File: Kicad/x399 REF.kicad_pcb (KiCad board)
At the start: 2 copper layers, 106 x 56 mm, 84 parts, among them J1 +15V, J2 Guard, J3 10Vref, Q1 MMBT3904, Q2 2SD882, Q3 AON7410, U1 LM399, U2 OP07

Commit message: Add files via upload
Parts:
- added F1alt1: RXEF010, OwnStuff:RXEF010, F.Cu at (71.0, 78.8)
- added R13alt1: 0.6W tht, Resistor_THT:R_Axial_DIN0309_L9.0mm_D3.2mm_P12.70mm_Horizontal, F.Cu at (167.4, 85.1)
- added R13alt2: 1206 smd, Resistor_SMD:R_1206_3216Metric_Pad1.30x1.75mm_HandSolder, F.Cu at (167.4, 91.4)
- added R25: 0R, Resistor_SMD:R_0805_2012Metric_Pad1.20x1.40mm_HandSolder, B.Cu at (136.6, 100.3)
- C18: value 100n NP0 -> 100n
- moved C9 17.1 mm to (143.6, 100.3)
- moved R6 17.1 mm to (143.6, 104.8)
- moved C3 16.7 mm to (136.6, 104.8), turned to -90 degrees
- moved R5 7.16 mm to (132.0, 87.0)
- moved R5alt1 5.92 mm to (125.4, 87.0)
- moved JP2 4.22 mm to (146.7, 85.0)
- moved H3 3.57 mm to (154.5, 101.3)
- moved JP1 3.57 mm to (144.5, 64.2)
- moved TP1 3.57 mm to (146.6, 68.7)
- moved C1 3.57 mm to (84.0, 76.0)
- moved C11 3.57 mm to (92.9, 70.6)
- moved C13 3.57 mm to (90.4, 72.0)
- moved C14 3.57 mm to (95.3, 65.0)
- moved C18 3.57 mm to (85.5, 98.5)
- moved C22 3.57 mm to (88.9, 108.5)
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- renumbered H3 to H1, H1 to H2, H2 to H3, R1alt1 to R5alt1
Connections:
- C3 pad 1: +10VREF -> Net-(C3-Pad1)
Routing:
- net MGND: track 343.1 -> 256.7 mm, vias 15 -> 22
- net +10VREF: track 300.7 -> 281.1 mm
- net Net-(R13-Pad2): track 62.6 -> 77.3 mm
- net Net-(JP2-A): track 12.5 -> 24.6 mm
- net Net-(U2A--): track 61.3 -> 71.2 mm
- net Net-(JP1-B): track 8.09 -> 16.0 mm
- net Net-(U2A-+): track 161.4 -> 154.6 mm
- net Net-(F1-Pad2): track 9.99 -> 15.0 mm
- net Net-(C3-Pad1): track 0.00 -> 4.12 mm
- net Net-(J1-Pin_1): track 6.47 -> 9.31 mm
- net Earth: track 83.8 -> 84.5 mm, vias 212 -> 200
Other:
- outline, holes or cut-outs redrawn
- board text added: "21-VII-2025"
- board text added: "REV {dblquote}A{dblquote}"
- board text removed: "10-VII-2025"

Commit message: Add files via upload
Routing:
- net Net-(U2A-+): track 154.6 -> 152.0 mm
- net Guard1: vias 0 -> 8
- added copper zone on F.Cu, net Guard1
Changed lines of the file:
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@@
 		(pcbplotparams
 			(layerselection 0x00000000_00000000_55555555_55555551)
-			(plot_on_all_layers_selection 0x00000000_00000000_00000080_02000002)
+			(plot_on_all_layers_selection 0x00000000_00000000_00000080_02000022)
 			(disableapertmacros no)
 			(usegerberextensions no)
@@
 		(sheetfile "x399 REF.kicad_sch")
 		(attr through_hole)
-		(fp_circle
-			(center -1.4 2.7)
-			(end -1.241886 2.700001)
-			(stroke
-				(width 0.1)
-				(type solid)
-			)
-			(fill yes)
-			(layer "F.SilkS")
-		)
 		(fp_line
 			(start 1.7 1.899999)
@@
 		(start 130.024013 92.5125)
 		(end 135.637177 98.125663)
-		(width 0.4)
+		(width 0.3)
 		(layer "B.Cu")
 		(net 1)
@@
 	)
 	(via
-		(at 154.781352 73.981488)
+		(at 154.663745 74.311151)
 		(size 0.8)
 		(drill 0.4)
@@
 	)
 	(via
-		(at 161.706352 73.079977)
+		(at 161.993297 73)
 		(size 0.8)
 		(drill 0.4)
@@
 	)
 	(via
-		(at 148.825 72.0125)
+		(at 148.860287 72.430401)
 		(size 0.8)
 		(drill 0.4)
@@
 	)
 	(via
-		(at 160.025 74.2625)
+		(at 159.886857 74.698048)
 		(size 0.8)
 		(drill 0.4)
@@
 		(start 134.019175 108.719311)
 		(end 130.557 112.181488)
-		(width 0.4)
+		(width 0.3)
 		(layer "B.Cu")
 		(net 2)
@@
 		(start 127.781352 112.181488)
 		(end 130.557 112.181488)
-		(width 0.4)
+		(width 0.3)
 		(layer "B.Cu")
 		(net 2)
@@
 		(start 151.683523 112.078977)
 		(end 149.590489 112.078977)
-		(width 0.4)
+		(width 0.3)
 		(layer "B.Cu")
 		(net 17)
@@
 	)
 	(segment
-		(start 150.981352 111.981488)
-		(end 149.493 111.981488)
-		(width 0.4)
-		(layer "B.Cu")
-		(net 17)
-	)
-	(segment
 		(start 156.481523 112.080977)
 		(end 163.7 104.8625)
@@
 	)
 	(segment
-		(start 149.693001 112.181488)
-		(end 150.781352 112.181488)
-		(width 0.3)
-		(layer "B.Cu")
-		(net 17)
-	)
-	(segment
 		(start 161.675 78.4125)
 		(end 161.675 74.464253)
@@
 		(start 149.493 111.981488)
 		(end 146.487176 108.975664)
-		(width 0.4)
+		(width 0.3)
 		(layer "B.Cu")
 		(net 17)
@@
 		(start 146.569175 96.169311)
 		(end 151.125 91.613487)
-		(width 0.4)
+		(width 0.3)
 		(layer "B.Cu")
 		(net 25)
@@
 		(net 38)
 	)
+	(via
+		(at 82 77.981488)
+		(size 0.8)
+		(drill 0.4)
+		(layers "F.Cu" "B.Cu")
+		(net 39)
+	)
+	(via
+		(at 80.55535 74)
+		(size 0.8)
+		(drill 0.4)
+		(layers "F.Cu" "B.Cu")
+		(net 39)
+	)
+	(via
+		(at 80.424431 72.575569)
+		(size 0.8)
+		(drill 0.4)
+		(layers "F.Cu" "B.Cu")
+		(net 39)
+	)
+	(via
+		(at 80.55535 77.5)
+		(size 0.8)
+		(drill 0.4)
+		(layers "F.Cu" "B.Cu")
+		(net 39)
+	)
+	(via
+		(at 80.71892 68.21892)
+		(size 0.8)
+		(drill 0.4)
+		(layers "F.Cu" "B.Cu")
+		(net 39)
+	)
+	(via
+		(at 79.281352 70)
+		(size 0.8)
+		(drill 0.4)
+		(layers "F.Cu" "B.Cu")
+		(net 39)
+	)
+	(via
+		(at 81.462432 76.537568)
+		(size 0.8)
+		(drill 0.4)
+		(layers "F.Cu" "B.Cu")
+		(net 39)
+	)
+	(via
+		(at 80.55535 75.5)
+		(size 0.8)
+		(drill 0.4)
+		(layers "F.Cu" "B.Cu")
+		(net 39)
+	)
 	(segment
 		(start 79.281352 69.481488)
-		(end 79.281352 70.231488)
+		(end 79.281352 70)
 		(width 1.5)
 		(layer "B.Cu")
@@
 	)
 	(segment
+		(start 80.55535 75.5)
+		(end 80.55535 74)
+		(width 2)
+		(layer "B.Cu")
+		(net 39)
+	)
+	(segment
+		(start 80.55535 77.5)
+		(end 80.55535 75.5)
+		(width 2)
+		(layer "B.Cu")
+		(net 39)
+	)
+	(segment
+		(start 80.71892 68.21892)
+		(end 83.931352 65.006488)
+		(width 2)
+		(layer "B.Cu")
+		(net 39)
+	)
+	(segment
 		(start 83.956352 77.981488)
-		(end 81.731352 77.981488)
+		(end 82 77.981488)
 		(width 2)
 		(layer "B.Cu")
@@
 	)
 	(segment
+		(start 80.55535 74)
+		(end 80.55535 72.706488)
+		(width 2)
+		(layer "B.Cu")
+		(net 39)
+	)
+	(segment
 		(start 86.103352 79.909488)
 		(end 86.103352 79.131488)
@@
 	(segment
 		(start 80.55535 72.706488)
-		(end 80.331352 72.48249)
+		(end 80.424431 72.575569)
 		(width 1.5)
 		(layer "B.Cu")
@@
 	)
 	(segment
+		(start 79.281352 70)
+		(end 79.281352 70.231488)
+		(width 1.5)
+		(layer "B.Cu")
+		(net 39)
+	)
+	(segment
 		(start 80.331352 71.281488)
 		(end 80.331352 70.456488)
@@
 	(segment
 		(start 80.55535 77.830488)
-		(end 80.55535 72.706488)
+		(end 80.55535 77.5)
 		(width 2)
 		(layer "B.Cu")
@@
 	(segment
 		(start 81.731352 76.806488)
-		(end 80.555351 75.630487)
+		(end 81.462432 76.537568)
 		(width 2)
 		(layer "B.Cu")
@@
 	)
 	(segment
+		(start 81.462432 76.537568)
+		(end 80.555351 75.630487)
+		(width 2)
+		(layer "B.Cu")
+		(net 39)
+	)
+	(segment
 		(start 83.956352 77.981488)
 		(end 83.956351 78.793987)
@@
 	)
 	(segment
+		(start 82 77.981488)
+		(end 81.731352 77.981488)
+		(width 2)
+		(layer "B.Cu")
+		(net 39)
+	)
+	(segment
 		(start 80.70635 77.981488)
 		(end 80.55535 77.830488)
@@
 	(segment
 		(start 80.331352 68.606488)
-		(end 83.931352 65.006488)
+		(end 80.71892 68.21892)
 		(width 2)
 		(layer "B.Cu")
@@
 	)
 	(segment
+		(start 80.424431 72.575569)
+		(end 80.331352 72.48249)
+		(width 1.5)
+		(layer "B.Cu")
+		(net 39)
+	)
+	(segment
 		(start 99.731352 107.266488)
 		(end 99.146352 107.266488)
@@
 	)
 	(zone
-		(net 2)
-		(net_name "Earth")
+		(net 39)
+		(net_name "Guard1")
 		(layer "F.Cu")
 		(hatch edge 0.5)
-		(priority 4)
+		(priority 5)
 		(connect_pads
-			(clearance 0.3)
+			(clearance 0.35)
 		)
-		(min_thickness 0.5)
+		(min_thickness 0.25)
 		(filled_areas_thickness no)
 		(fill yes
-			(thermal_gap 0.3)
+			(thermal_gap 0.5)
 			(thermal_bridge_width 0.5)
 		)
 		(polygon
 			(pts
-				(xy 80.981352 86.581488) (xy 100 86) (xy 106 80) (xy 106 78) (xy 106 74) (xy 106 71) (xy 106 67.5)
-				(xy 106 63) (xy 105.5 59.5) (xy 95.981352 59.581488) (xy 90.4 74.1) (xy 92.6 80.1) (xy 87.156352 79.881488)
-				(xy 79.981352 78.581488)
+				(xy 83.5 78.5) (xy 82 77) (xy 82 75.5) (xy 81.5 75) (xy 81.5 69) (xy 84.5 69) (xy 86 67.5) (xy 85 66.075136)
+				(xy 83.931352 65.006488) (xy 81 64) (xy 78.5 66.506488) (xy 78.5 70.5) (xy 79.5 71.5) (xy 79.522282 78.154766)
+				(xy 80.367516 79) (xy 83 79)
 			)
 		)
 	)
 	(zone
-		(net 0)
-		(net_name "")
-		(layers "F.Cu" "B.Cu")
+		(net 2)
+		(net_name "Earth")
+		(layer "F.Cu")
 		(hatch edge 0.5)
-		(connect_pads yes
-			(clearance 0)
+		(priority 4)
+		(connect_pads
+			(clearance 0.3)
 		)
-		(min_thickness 0.25)
+		(min_thickness 0.5)
 		(filled_areas_thickness no)
-		(keepout
-			(tracks allowed)
-			(vias allowed)
-			(pads allowed)
-			(copperpour not_allowed)
-			(footprints allowed)
-		)
-		(placement
-			(enabled no)
-			(sheetname "/")
-		)
-		(fill
-			(thermal_gap 0.5)
+		(fill yes
+			(thermal_gap 0.3)
 			(thermal_bridge_width 0.5)
 		)
 		(polygon
 			(pts
-				(xy 75.681352 58.481488) (xy 76.181352 58.281488) (xy 88.181352 58.281488) (xy 88.181352 69.481488)
-				(xy 75.181352 69.481488) (xy 75.181352 58.481488)
+				(xy 80.981352 86.581488) (xy 100 86) (xy 106 80) (xy 106 78) (xy 106 74) (xy 106 71) (xy 106 67.5)
+				(xy 106 63) (xy 105.5 59.5) (xy 95.981352 59.581488) (xy 90.4 74.1) (xy 92.6 80.1) (xy 83.450319 80.5)
+				(xy 81.5 80.5)
 			)
 		)
@@
 		(polygon
 			(pts
-				(xy 71.706361 69.581488) (xy 87.156352 69.581488) (xy 87.156352 79.881488) (xy 80.856352 79.881488)
-				(xy 77.956355 82.781485) (xy 78.100721 74.696982)
+				(xy 39.655232 54.607361) (xy 55.105223 54.607361) (xy 55.105223 64.907361) (xy 48.805223 64.907361)
+				(xy 45.905226 67.807358) (xy 46.049592 59.722855)
 			)
 		)
@@
 		(polygon
 			(pts
-				(xy 80.056351 70.481488) (xy 73.681352 70.581488) (xy 70.381352 70.781488) (xy 67.181352 72.981488)
-				(xy 67.581352 94.081488) (xy 69.281352 94.481488) (xy 79.581352 94.481488) (xy 79.681352 86.781488)
-				(xy 79.781352 86.381488) (xy 80.056351 71.281488)
+				(xy 78.5 70.5) (xy 73.681352 70.581488) (xy 70.381352 70.781488) (xy 67.181352 72.981488) (xy 67.581352 94.081488)
+				(xy 69.281352 94.481488) (xy 79.581352 94.481488) (xy 79.681352 86.781488) (xy 79.781352 86.381488)
+				(xy 79.5 78.5) (xy 79.5 71.5)
 			)
 		)
@@
 			)
 		)
+	)
+	(zone
+		(net 0)
+		(net_name "")
+		(layer "B.Cu")
+		(hatch edge 0.5)
+		(connect_pads yes
+			(clearance 0)
+		)
+		(min_thickness 0.25)
+		(filled_areas_thickness no)
+		(keepout
+			(tracks allowed)
+			(vias allowed)
+			(pads allowed)
+			(copperpour not_allowed)
+			(footprints allowed)
+		)
+		(placement
+			(enabled no)
+			(sheetname "/")
+		)
+		(fill
+			(thermal_gap 0.5)
+			(thermal_bridge_width 0.5)
+		)
+		(polygon
+			(pts
+				(xy 75.681352 58.481488) (xy 76.181352 58.281488) (xy 88.181352 58.281488) (xy 88.181352 69.481488)
+				(xy 75.181352 69.481488) (xy 75.181352 58.481488)
+			)
+		)

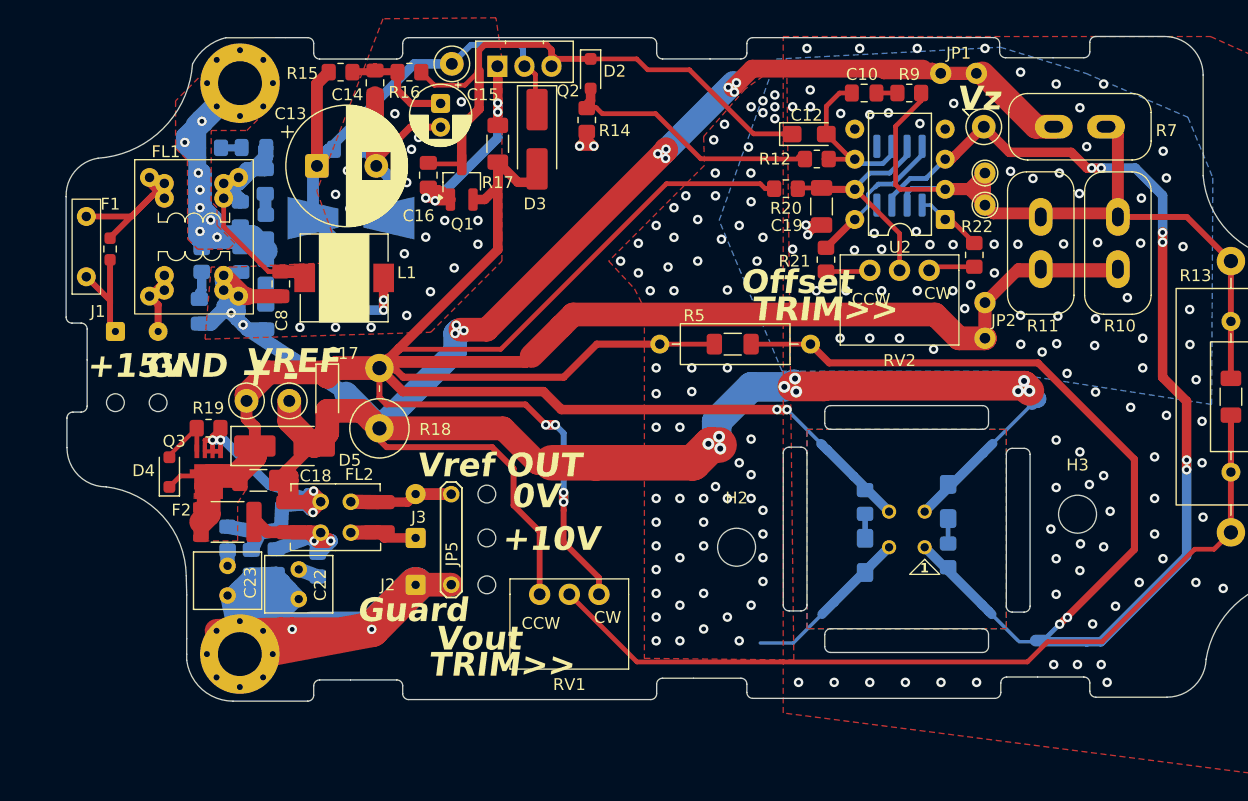
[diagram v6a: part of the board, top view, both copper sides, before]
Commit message: Add files via upload
Replaced guard2 1u film capacitors for more accessible ones, improved thermal design on output
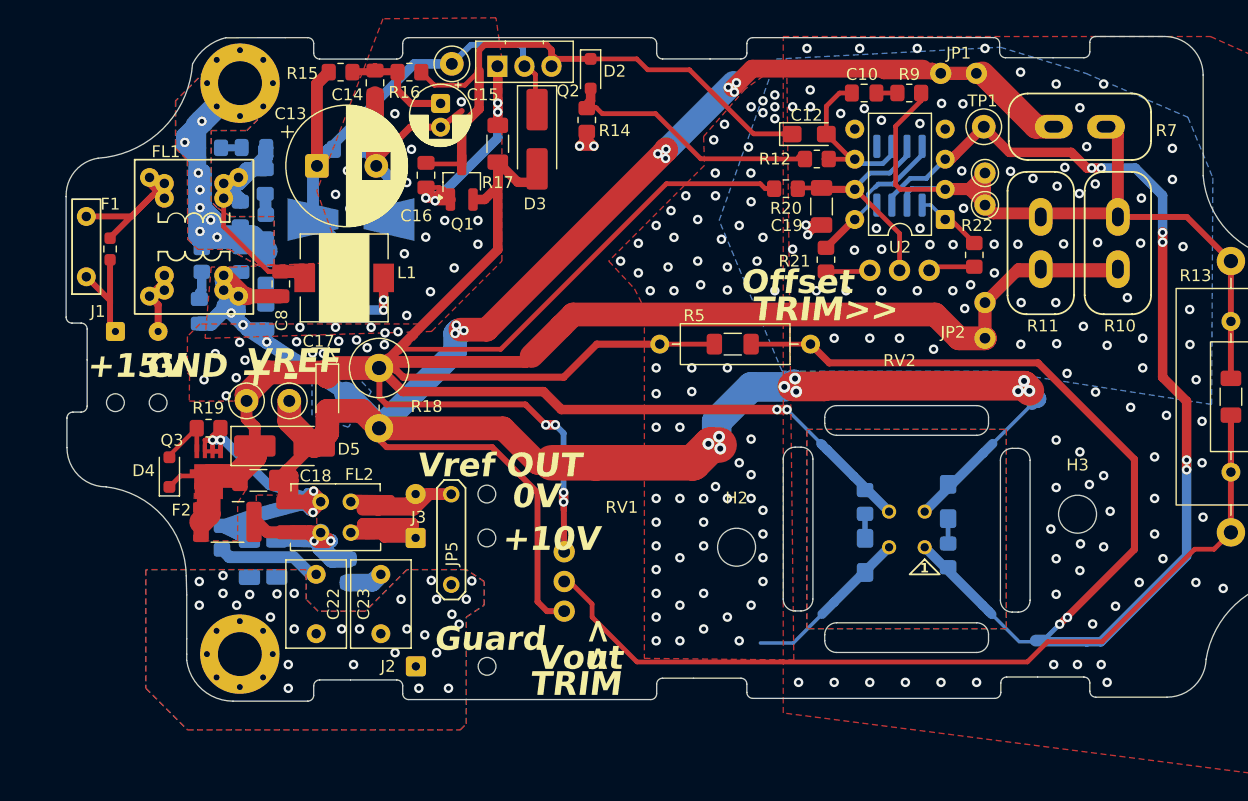
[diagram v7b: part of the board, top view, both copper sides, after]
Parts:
- C20, C21: footprint Capacitor_SMD:C_0805_2012Metric_Pad1.18x1.45mm_HandSolder -> Capacitor_SMD:C_1206_3216Metric_Pad1.33x1.80mm_HandSolder
- C22, C23: footprint Capacitor_THT:C_Rect_L4.6mm_W5.5mm_P2.50mm_MKS02_FKP02 -> OwnStuff:C_Rect_L7.2mm_W5mm_P5.00mm_FKS2_FKP2_MKS2_MKP2
- R21, R22: value 10k -> 10k PTF
- moved C22 7.51 mm to (95.8, 111.4)
- moved C23 7.50 mm to (90.3, 106.4)
- moved J2 6.87 mm to (98.8, 114.2)
- moved R18 5.09 mm to (95.7, 89.0), turned to -90 degrees
- moved R23 2.62 mm to (93.0, 106.1)
- moved RV1 2.51 mm to (111.2, 109.5), turned to -90 degrees
- moved R24 0.48 mm to (82.4, 103.3)
- moved C21 0.35 mm to (84.7, 105.1)
- moved C20 0.27 mm to (87.0, 105.0)
- moved C16 0.20 mm to (99.6, 72.8)
- moved D1 0.12 mm to (93.3, 76.5)
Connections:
- R18 pad 1: MGND -> +10VREF
- R18 pad 2: +10VREF -> MGND
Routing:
- net Guard2: track 110.7 -> 0.00 mm, vias 2 -> 28
- net Net-(J3-Pin_1): track 6.03 -> 16.9 mm
- net Net-(C23-Pad1): track 1.30 -> 8.81 mm
- net Net-(J3-Pin_2): track 8.54 -> 15.4 mm
- net MGND: track 256.7 -> 263.2 mm
- net Net-(JP3-A): track 15.9 -> 22.3 mm
- net +10VREF: track 281.1 -> 277.7 mm
- net Earth: track 84.5 -> 86.8 mm, vias 200 -> 223
- net Net-(R13-Pad2): track 77.3 -> 78.8 mm
- net Net-(C22-Pad2): track 1.71 -> 3.04 mm
- added copper zone on B.Cu, net Guard1
- added copper zone on B.Cu, net Guard2
- added copper zone on F.Cu, net Guard2
- added copper zone on F.Cu, net MGND
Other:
- outline, holes or cut-outs redrawn
- board text added: ">>"
- board text added: "TP1"
- board text added: "TRIM"
- board text removed: "Vz"

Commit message: Add files via upload
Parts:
- moved F1alt1 1.69 mm to (72.6, 79.0)
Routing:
- net MGND: track 263.2 -> 275.1 mm
- net +10VREF: track 277.7 -> 286.7 mm
- net Net-(J1-Pin_1): track 9.31 -> 6.22 mm
- net Earth: vias 223 -> 230
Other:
- board size 106 x 56 mm -> 105.7 x 56 mm
